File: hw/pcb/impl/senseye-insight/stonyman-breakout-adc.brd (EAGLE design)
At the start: 31 x 9.4 mm, 8 parts

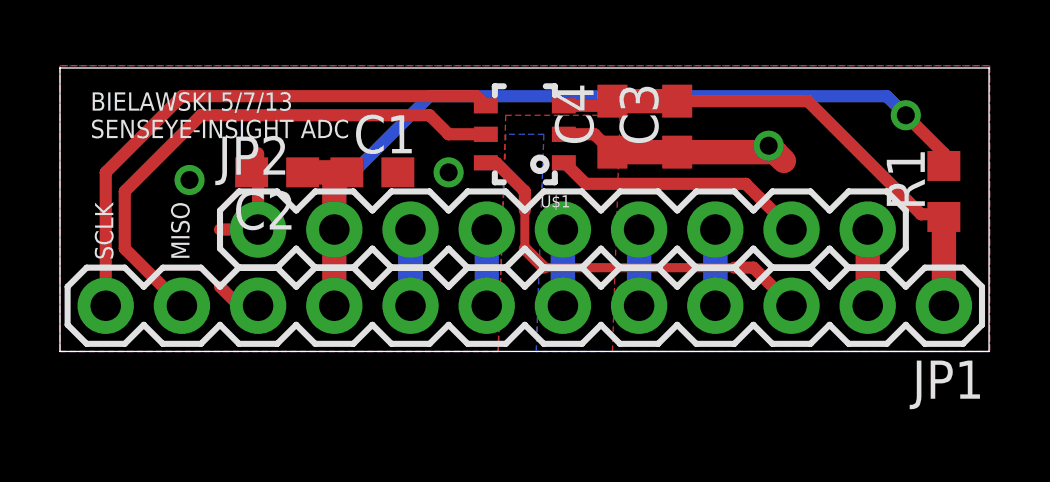
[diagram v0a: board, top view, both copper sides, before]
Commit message: added silkscreen text for all new inputs
SCLK, MISO, CS and VADC
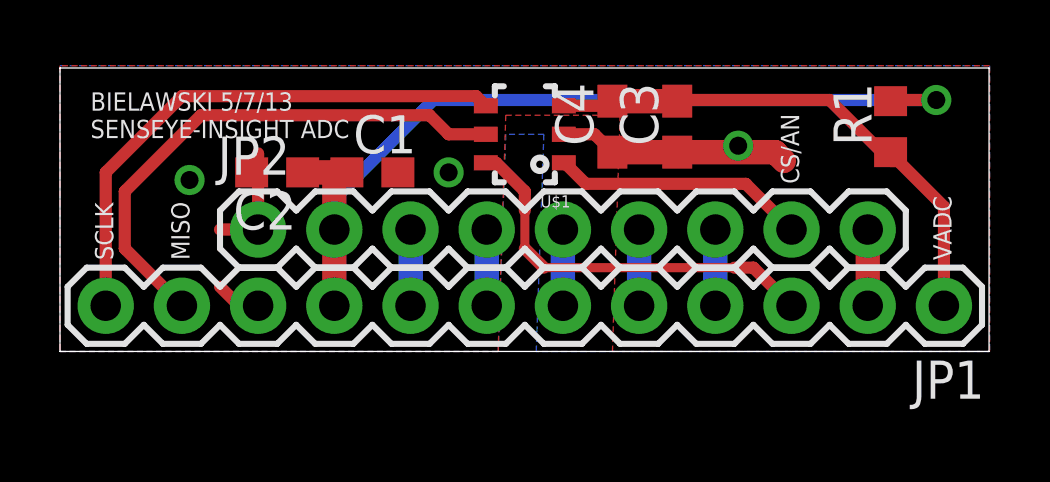
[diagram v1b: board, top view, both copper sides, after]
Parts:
- moved R1 2.80 mm to (27.7, 7.49)
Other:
- board text added: "CS/AN"
- board text added: "VADC"
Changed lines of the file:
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@@
 <text x="1.778" y="3.048" size="0.6096" layer="21" rot="R90">SCLK</text>
 <text x="4.318" y="3.048" size="0.6096" layer="21" rot="R90">MISO</text>
+<text x="29.718" y="3.048" size="0.6096" layer="21" rot="R90">VADC</text>
+<text x="24.638" y="5.588" size="0.6096" layer="21" rot="R90">CS/AN</text>
 </plain>
 <attributes>
@@
 <element name="C3" library="rcl" package="C0603" value="0.1uF" x="20.574" y="7.493" rot="R90"/>
 <element name="C4" library="rcl" package="C0603" value="1uF" x="18.415" y="7.493" rot="R90"/>
-<element name="R1" library="rcl" package="R0603" value="0 or UNPOP" x="29.464" y="5.334" rot="R90"/>
+<element name="R1" library="rcl" package="R0603" value="0 or UNPOP" x="27.686" y="7.493" rot="R90"/>
 <element name="JP1" library="SparkFun-Connectors" package="1X12" value="M12PTH" x="29.464" y="1.524" rot="R180"/>
 <element name="JP2" library="SparkFun-Connectors" package="1X09" value="M09" x="6.604" y="4.064"/>
@@
 <wire x1="18.415" y1="6.643" x2="23.837" y2="6.643" width="0.8128" layer="1"/>
 <wire x1="23.837" y1="6.643" x2="24.13" y2="6.35" width="0.8128" layer="1"/>
-<via x="23.622" y="6.858" extent="1-16" drill="0.6"/>
+<via x="22.606" y="6.858" extent="1-16" drill="0.6"/>
 </signal>
 <signal name="V_STONY">
@@
 <wire x1="9.564" y1="5.969" x2="9.144" y2="5.969" width="0.8128" layer="1"/>
 <wire x1="9.144" y1="5.969" x2="9.144" y2="4.064" width="0.8128" layer="1"/>
-<wire x1="29.464" y1="6.184" x2="29.464" y2="6.604" width="0.4064" layer="1"/>
-<wire x1="29.464" y1="6.604" x2="28.194" y2="7.874" width="0.4064" layer="1"/>
-<via x="28.194" y="7.874" extent="1-16" drill="0.6"/>
-<wire x1="28.194" y1="7.874" x2="27.559" y2="8.509" width="0.4064" layer="16"/>
-<wire x1="27.559" y1="8.509" x2="12.319" y2="8.509" width="0.4064" layer="16"/>
-<wire x1="12.319" y1="8.509" x2="9.144" y2="5.334" width="0.4064" layer="16"/>
-<wire x1="9.144" y1="5.334" x2="9.144" y2="4.064" width="0.4064" layer="16"/>
+<wire x1="27.686" y1="8.343" x2="27.725" y2="8.382" width="0.4064" layer="1"/>
+<wire x1="27.725" y1="8.382" x2="29.21" y2="8.382" width="0.4064" layer="1"/>
+<via x="29.21" y="8.382" extent="1-16" drill="0.6"/>
+<wire x1="29.21" y1="8.382" x2="12.446" y2="8.382" width="0.4064" layer="16"/>
+<wire x1="12.446" y1="8.382" x2="9.144" y2="5.08" width="0.4064" layer="16"/>
+<wire x1="9.144" y1="5.08" x2="9.144" y2="4.064" width="0.4064" layer="16"/>
 </signal>
 <signal name="RESP">
@@
 <contactref element="R1" pad="1"/>
 <contactref element="JP1" pad="1"/>
-<wire x1="29.464" y1="1.524" x2="29.464" y2="4.484" width="0.8128" layer="1"/>
 <wire x1="16.794" y1="8.189" x2="18.261" y2="8.189" width="0.4064" layer="1"/>
 <wire x1="18.261" y1="8.189" x2="18.415" y2="8.343" width="0.4064" layer="1"/>
 <wire x1="18.415" y1="8.343" x2="20.574" y2="8.343" width="0.8128" layer="1"/>
-<wire x1="20.574" y1="8.343" x2="24.931" y2="8.343" width="0.4064" layer="1"/>
-<wire x1="24.931" y1="8.343" x2="28.702" y2="4.572" width="0.4064" layer="1"/>
-<wire x1="28.702" y1="4.572" x2="29.376" y2="4.572" width="0.4064" layer="1"/>
-<wire x1="29.376" y1="4.572" x2="29.464" y2="4.484" width="0.4064" layer="1"/>
+<wire x1="29.464" y1="1.524" x2="29.464" y2="4.826" width="0.4064" layer="1"/>
+<wire x1="29.464" y1="4.826" x2="27.94" y2="6.35" width="0.4064" layer="1"/>
+<wire x1="27.94" y1="6.35" x2="27.686" y2="6.35" width="0.4064" layer="1"/>
+<wire x1="27.686" y1="6.35" x2="25.654" y2="8.382" width="0.4064" layer="1"/>
+<wire x1="25.654" y1="8.382" x2="20.613" y2="8.382" width="0.4064" layer="1"/>
+<wire x1="20.613" y1="8.382" x2="20.574" y2="8.343" width="0.4064" layer="1"/>
+<wire x1="27.686" y1="6.35" x2="27.686" y2="6.643" width="0" layer="19" extent="1-1"/>
 </signal>
 <signal name="ANALOG">
